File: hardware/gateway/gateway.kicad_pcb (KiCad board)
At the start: 2 copper layers, 65 x 32 mm, 31 parts, among them J1 FTDI, J2 Conn_Coaxial, J3 Raspberry_Pi_2_3, U1 RFM69HW, U2 DS1307Z+, U3 AP130-xxY, Y1 32768

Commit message: Updated date
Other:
- board text added: "OOS 2019-08-25"
- board text removed: "OOS 2019-06-24"
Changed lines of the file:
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@@
     (pcbplotparams
       (layerselection 0x010fc_ffffffff)
-      (usegerberextensions false)
+      (usegerberextensions true)
       (usegerberattributes false)
       (usegerberadvancedattributes false)
@@
       (outputformat 1)
       (mirror false)
-      (drillshape 1)
+      (drillshape 0)
       (scaleselection 1)
-      (outputdirectory ""))
+      (outputdirectory "gerbers/"))
   )
   (net 0 "")
@@
     (effects (font (size 1 1) (thickness 0.2)) (justify mirror))
   )
-  (gr_text "OOS 2019-06-24" (at 160.25 61.5 90) (layer B.SilkS)
+  (gr_text "OOS 2019-08-25" (at 160.25 61.5 90) (layer B.SilkS)
     (effects (font (size 1 1) (thickness 0.2)) (justify mirror))
   )

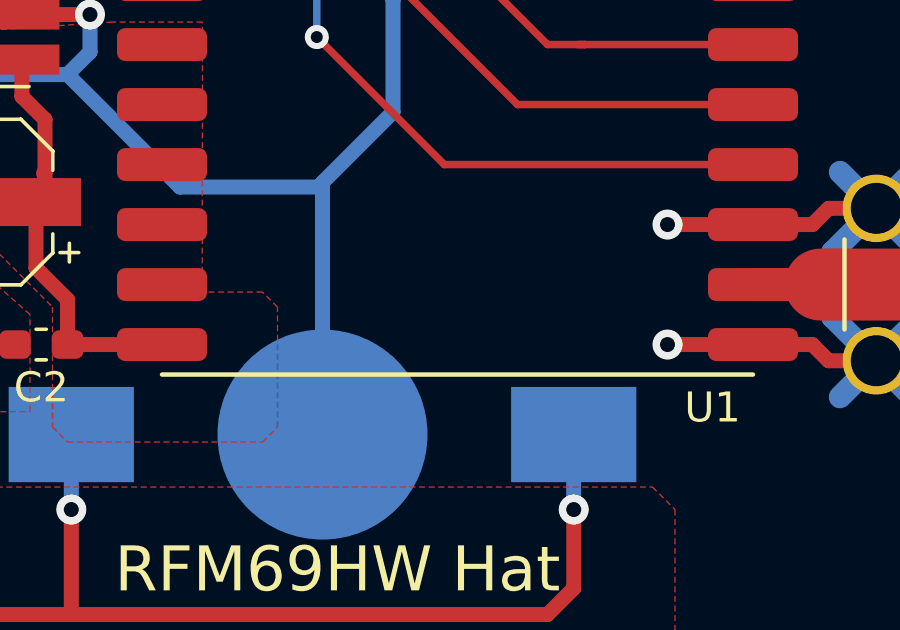
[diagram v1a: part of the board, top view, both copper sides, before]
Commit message: Add silkscreen for JLCPCB order number
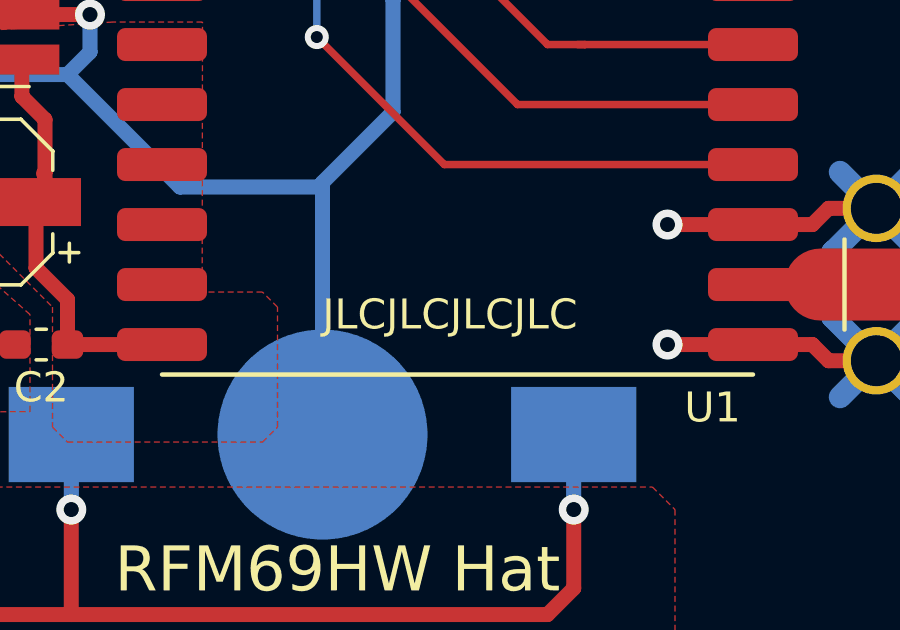
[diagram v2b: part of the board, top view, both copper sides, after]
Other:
- board text added: "JLCJLCJLCJLC"
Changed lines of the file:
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@@
   (general
     (thickness 1.6)
-    (drawings 21)
+    (drawings 22)
     (tracks 317)
     (zones 0)
@@
     )
   )
+  (gr_text JLCJLCJLCJLC (at 137.25 64.75) (layer F.SilkS)
+    (effects (font (size 1 1) (thickness 0.2)))
+  )
   (gr_text GND (at 119.25 74.75) (layer B.SilkS)
